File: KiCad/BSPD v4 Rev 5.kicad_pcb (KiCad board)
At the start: 4 copper layers, 100 x 77.5 mm, 194 parts, among them J1 DTM13-12PA, U1 LM339, U10 2N7002, U11 2N7002, U12 2N7002, U13 2N7002, U14 2N7002, U15 2N7002, U16 2N7002, U17 74HC08D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

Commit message: Changed DTM NPTH size
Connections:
- U18 pad 11: (no net) -> unconnected-(U18-Pad11)
- U18 pad 3: (no net) -> unconnected-(U18-Pad3)
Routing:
- net BSPD_status(12V): track 79.0 -> 93.1 mm
- net Net-(U2C--): track 112.2 -> 118.8 mm
- net GND: vias 279 -> 278
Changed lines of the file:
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@@
 			(outputformat 1)
 			(mirror no)
-			(drillshape 1)
+			(drillshape 0)
 			(scaleselection 1)
-			(outputdirectory "")
+			(outputdirectory "../Production/Fab (gerber) BSPD v4 Rev 5/")
 		)
 	)
@@
 	(net 113 "unconnected-(U25C-Q3-Pad10)")
 	(net 114 "unconnected-(U25B-Q2-Pad9)")
+	(net 115 "unconnected-(U18-Pad3)")
+	(net 116 "unconnected-(U18-Pad11)")
 	(footprint "Resistor_SMD:R_0805_2012Metric_Pad1.20x1.40mm_HandSolder"
 		(layer "F.Cu")
@@
 			(at -8.89 -12.7 90)
 			(size 5 5)
-			(drill 3)
-			(layers "F&B.Cu" "*.Mask")
+			(drill 5)
+			(layers "*.Mask")
 		)
 		(pad "" np_thru_hole circle
 			(at 8.89 -12.7 90)
 			(size 5 5)
-			(drill 3)
-			(layers "F&B.Cu" "*.Mask")
+			(drill 5)
+			(layers "*.Mask")
 		)
 		(pad "1" thru_hole roundrect
@@
 		)
 		(group ""
-			(members "0762a500-42f2-42fb-a078-6c1aa5e056fa" "084b3688-b081-4450-aacb-739ad2118ab8"
-				"0d6cd142-b1c8-48ca-ac65-122be22d51ec" "198ef3f8-6b8f-4339-8e8e-52dd78860bf9"
-				"20b9208b-f209-438b-9e0c-cbd13adca767" "492f48d9-6674-48c5-9826-66c5159c251b"
-				"49af12c1-a1eb-4583-9b77-ae47ca6a3e2e" "651534ea-3f12-4366-9872-520313e98250"
-				"7ad67e8d-3dc0-490f-9ea3-ee7503f5d862" "7db140bb-23d2-4ea7-861f-e28e8502dec4"
-				"848d9453-0247-48af-83de-b9f01f822996" "8ba0055a-b60d-4a51-a8c9-ef2f70b57686"
-				"99198183-94ea-4d01-9891-043bd2b0469f" "ab4a9615-9050-4230-b962-8291ca35c75c"
-				"bc787465-82ed-4e8a-a340-4af8fc745ab3" "bda766bf-56de-4e9e-a06b-fc5527dfb734"
-				"d74cc8b5-ec6e-48dc-a64b-0fa3fd9d8ad2" "d878d63a-22b1-43e1-82f4-1738e3ae9442"
-				"db3fa60b-dd23-4084-b817-4ca42268c97e" "e277162a-7d40-42ac-b809-249cfe4dc1e0"
-				"e35fbb23-64cf-4d94-aa0a-6c12e2d1ecf5" "e5b0d9e6-d4bd-4c73-8cac-be1be8c46e06"
+			(members "2a8d6c05-4f68-4065-8f50-f404b86ca30a" "2b647277-423f-45bb-b5af-bc07fde5212c"
+				"2bddd831-3458-409e-bcb9-7c070f0f1419" "32dc1de1-0e17-4066-abfa-8d649ab330a1"
+				"4bfcb310-1cd9-4686-b639-f17e350bee0d" "4d9337d3-cba9-47d8-9d35-7dbac8836a1c"
+				"827f3cdf-d24f-4c54-822c-144fb845f094" "8bbaeb87-f568-4227-8b07-fff5f8ed2c97"
+				"916b219d-f275-4fb5-b2ef-d5d6e7277683" "94bab4a8-2b81-48eb-b3a7-0c39814db9f9"
+				"94d2f2b8-f4b8-45f6-899a-d1736687bf8b" "9807fecc-2b0b-49ce-8c03-c772a7bd696e"
+				"ab198cf8-ebde-45a8-8071-e6fe45066953" "d2159468-2c08-406f-827d-736941325d98"
+				"d5026557-77fd-4762-9f81-bd560b215afa" "e3873f4e-5db2-4c4e-a76c-aa21f2ea86fa"
+				"eb1fc0db-555f-4578-958b-a648d1696b06" "f213b850-67e0-4ee2-b7f8-166f49001d37"
+				"f22a5232-f775-44e7-a3a7-72842215190f" "fd43b7fc-b80b-4804-a2f5-b0c0e8812592"
+				"fda41aae-57ef-41ab-9ef1-84b8804f4714" "ff72e685-8ea9-41a7-82c6-c40ddcfb733d"
 			)
 		)
@@
 			(layers "F.Cu" "F.Mask" "F.Paste")
 			(roundrect_rratio 0.25)
+			(net 115 "unconnected-(U18-Pad3)")
 			(pinfunction "3")
 			(pintype "no_connect")
@@
 			(layers "F.Cu" "F.Mask" "F.Paste")
 			(roundrect_rratio 0.25)
+			(net 116 "unconnected-(U18-Pad11)")
 			(pinfunction "11")
 			(pintype "no_connect")
@@
 	)
 	(via
-		(at 177.4 112.7)
-		(size 0.6)
-		(drill 0.3)
-		(layers "F.Cu" "B.Cu")
-		(free yes)
-		(net 1)
-	)
-	(via
 		(at 179 77)
 		(size 0.6)
@@
 	)
 	(segment
-		(start 151.65 112.54)
-		(end 150.289 113.901)
-		(width 0.2)
-		(layer "F.Cu")
-		(net 21)
-	)
-	(segment
 		(start 169.25 139.05)
 		(end 177.8 139.05)
@@
 	)
 	(segment
-		(start 150.289 113.901)
-		(end 150.289 131.039)
-		(width 0.2)
-		(layer "F.Cu")
-		(net 21)
-	)
-	(segment
 		(start 201.755888 136.55)
 		(end 200.827944 137.477944)
@@
 	)
 	(segment
-		(start 158.3 139.05)
-		(end 169.25 139.05)
-		(width 0.2)
-		(layer "F.Cu")
-		(net 21)
-	)
-	(segment
 		(start 180.25 141.5)
 		(end 180.5 141.5)
@@
 	)
 	(segment
-		(start 150.289 131.039)
-		(end 158.3 139.05)
+		(start 180.25 141.5)
+		(end 177.75 139)
 		(width 0.2)
-		(layer "F.Cu")
+		(layer "In2.Cu")
+		(net 21)
+	)
+	(segment
+		(start 149.5 114.69)
+		(end 151.65 112.54)
+		(width 0.2)
+		(layer "In2.Cu")
+		(net 21)
+	)
+	(segment
+		(start 180.5 141.5)
+		(end 180.25 141.5)
+		(width 0.2)
+		(layer "In2.Cu")
+		(net 21)
+	)
+	(segment
+		(start 156.25 139)
+		(end 149.5 132.25)
+		(width 0.2)
+		(layer "In2.Cu")
+		(net 21)
+	)
+	(segment
+		(start 149.5 132.25)
+		(end 149.5 114.69)
+		(width 0.2)
+		(layer "In2.Cu")
+		(net 21)
+	)
+	(segment
+		(start 177.75 139)
+		(end 156.25 139)
+		(width 0.2)
+		(layer "In2.Cu")
 		(net 21)
 	)
@@
 	)
 	(segment
-		(start 149 131.75)
-		(end 149 106.8)
+		(start 149.4 106.4)
+		(end 151.65 104.15)
 		(width 1)
 		(layer "In1.Cu")
@@
 	)
 	(segment
-		(start 185.15 141.5)
-		(end 182.4 138.75)
+		(start 149.4 132.15)
+		(end 149.4 106.4)
 		(width 1)
 		(layer "In1.Cu")
@@
 	(segment
 		(start 156 138.75)
-		(end 149 131.75)
+		(end 149.4 132.15)
 		(width 1)
 		(layer "In1.Cu")
@@
 	)
 	(segment
-		(start 149 106.8)
-		(end 151.65 104.15)
+		(start 185.15 141.5)
+		(end 182.4 138.75)
 		(width 1)
 		(layer "In1.Cu")
@@
 	)
 	(segment
-		(start 158.75 141.5)
-		(end 174.2 141.5)
+		(start 149.4 110.6)
+		(end 149.4 132.15)
 		(width 1)
 		(layer "F.Cu")
@@
 	)
 	(segment
-		(start 149 131.75)
-		(end 158.75 141.5)
+		(start 151.65 108.35)
+		(end 149.4 110.6)
 		(width 1)
 		(layer "F.Cu")
@@
 	)
 	(segment
-		(start 149 111)
-		(end 149 131.75)
+		(start 149.4 132.15)
+		(end 158.75 141.5)
 		(width 1)
 		(layer "F.Cu")
@@
 	)
 	(segment
-		(start 151.65 108.35)
-		(end 149 111)
+		(start 158.75 141.5)
+		(end 174.2 141.5)
 		(width 1)
 		(layer "F.Cu")
@@
 	)
 	(segment
-		(start 174.04 109.54)
-		(end 174.5 110)
+		(start 226 83.75)
+		(end 227 84.75)
 		(width 0.2)
 		(layer "F.Cu")
@@
 	)
 	(segment
-		(start 174.5 110)
-		(end 176 110)
+		(start 171.5 111.5)
+		(end 172.5 111.5)
 		(width 0.2)
 		(layer "F.Cu")
@@
 	)
 	(segment
-		(start 226 83.75)
-		(end 227 84.75)
+		(start 172.5 111.5)
+		(end 174.04 109.96)
 		(width 0.2)
 		(layer "F.Cu")
@@
 	)
 	(segment
-		(start 174.04 108.725)
-		(end 174.04 109.54)
+		(start 214.416667 71.75)
+		(end 217 71.75)
 		(width 0.2)
 		(layer "F.Cu")
@@
 	)
 	(segment
-		(start 214.416667 71.75)
-		(end 217 71.75)
+		(start 174.04 109.96)
+		(end 174.04 108.725)
 		(width 0.2)
 		(layer "F.Cu")
@@
 	)
 	(via
-		(at 176 110)
+		(at 171.5 111.5)
 		(size 0.6)
 		(drill 0.3)
@@
 	)
 	(segment
-		(start 227 85.5)
+		(start 227 75.25)
 		(end 227 84.75)
 		(width 0.2)
@@
 	)
 	(segment
-		(start 227 75.25)
-		(end 227 84.75)
+		(start 233 91.5)
+		(end 233 102)
 		(width 0.2)
 		(layer "In2.Cu")
@@
 	)
 	(segment
-		(start 233 91.5)
+		(start 227 84.75)
 		(end 227 85.5)
 		(width 0.2)
@@
 	)
 	(segment
+		(start 233 102)
+		(end 225.5 109.5)
+		(width 0.2)
+		(layer "In2.Cu")
+		(net 59)
+	)
+	(segment
 		(start 217 71.75)
 		(end 223.5 71.75)
@@
 	)
 	(segment
-		(start 233 102)
-		(end 233 91.5)
+		(start 172.5 111.5)
+		(end 171.5 111.5)
 		(width 0.2)
 		(layer "In2.Cu")
@@
 	)
 	(segment
-		(start 176 110)
-		(end 176.5 109.5)
+		(start 223.5 71.75)
+		(end 227 75.25)
 		(width 0.2)
 		(layer "In2.Cu")
@@
 	)
 	(segment
-		(start 176.5 109.5)
-		(end 225.5 109.5)
+		(start 225.5 109.5)
+		(end 174.5 109.5)
 		(width 0.2)
 		(layer "In2.Cu")
@@
 	)
 	(segment
-		(start 223.5 71.75)
-		(end 227 75.25)
+		(start 174.5 109.5)
+		(end 172.5 111.5)
 		(width 0.2)
 		(layer "In2.Cu")
@@
 	)
 	(segment
-		(start 225.5 109.5)
-		(end 233 102)
+		(start 227 85.5)
+		(end 233 91.5)
 		(width 0.2)
 		(layer "In2.Cu")

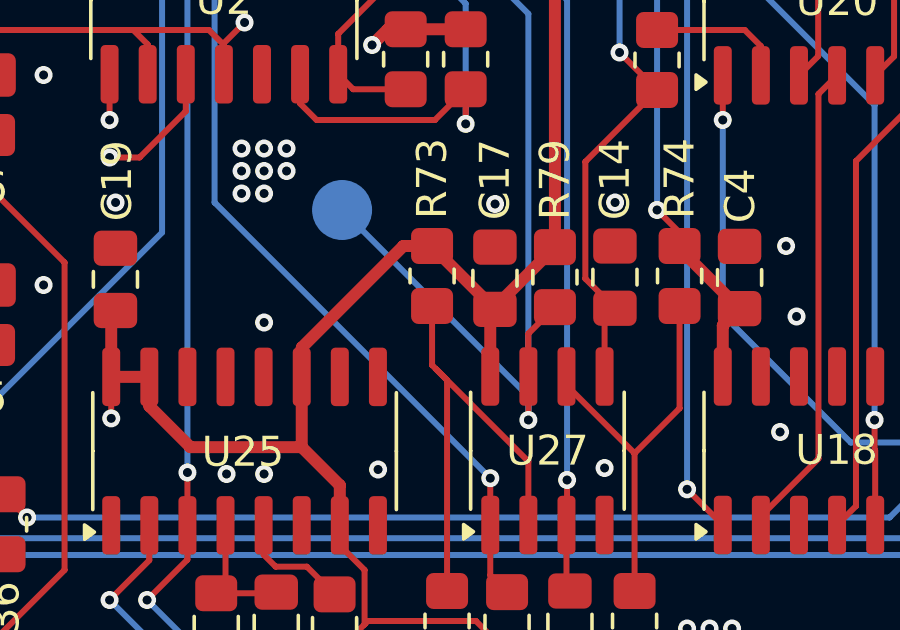
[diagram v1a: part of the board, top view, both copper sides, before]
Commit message: moved lm393 to 12v
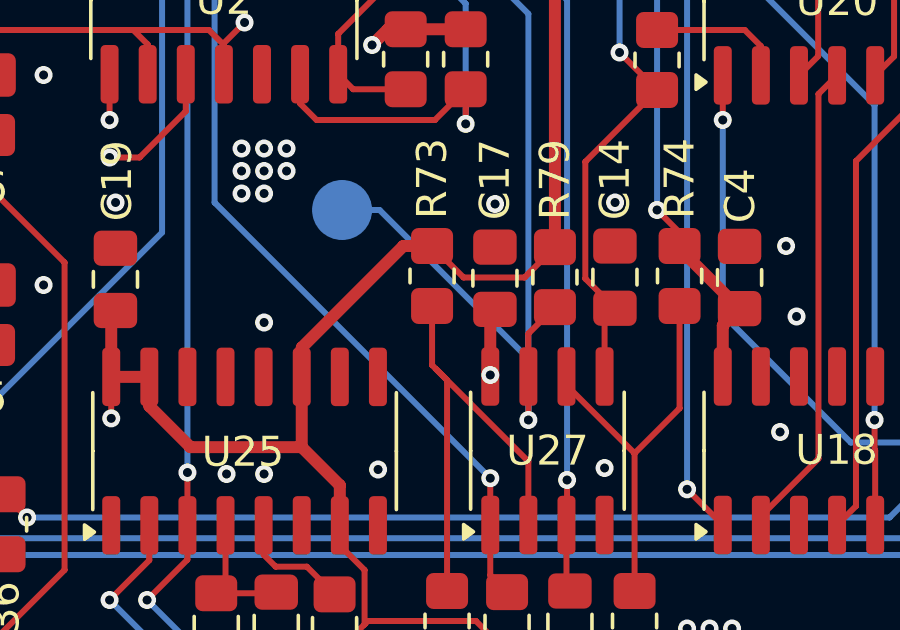
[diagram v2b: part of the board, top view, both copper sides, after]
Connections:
- C17 pad 1: +5V -> +12V
- U27 pad 8: +5V -> +12V
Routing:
- net +12V: track 303.8 -> 322.4 mm, vias 4 -> 5
- net +5V: track 533.6 -> 530.4 mm
- net Net-(U21C-3B): track 48.4 -> 49.1 mm
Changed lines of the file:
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@@
 			(drillshape 0)
 			(scaleselection 1)
-			(outputdirectory "../Production/Fab (gerber) BSPD v4 Rev 5/")
+			(outputdirectory "../Production/Fab/")
 		)
 	)
@@
 			(layers "F.Cu" "F.Mask" "F.Paste")
 			(roundrect_rratio 0.25)
-			(net 2 "+5V")
+			(net 6 "+12V")
 			(pinfunction "V+")
 			(pintype "power_in")
@@
 			(layers "F.Cu" "F.Mask" "F.Paste")
 			(roundrect_rratio 0.212766)
-			(net 2 "+5V")
+			(net 6 "+12V")
 			(pintype "passive")
 		)
@@
 	)
 	(segment
-		(start 184.345 116.4875)
-		(end 186.345 114.4875)
-		(width 0.4)
-		(layer "F.Cu")
-		(net 2)
-	)
-	(segment
 		(start 155 80.5)
 		(end 158.25 77.25)
@@
 	)
 	(segment
-		(start 184.19 118.8)
-		(end 184.19 116.7175)
-		(width 0.4)
-		(layer "F.Cu")
-		(net 2)
-	)
-	(segment
 		(start 187.59375 103.90625)
 		(end 187.6875 103.8125)
@@
 	)
 	(segment
-		(start 182.25 114.4675)
-		(end 184.345 116.5625)
-		(width 0.4)
-		(layer "F.Cu")
-		(net 2)
-	)
-	(segment
 		(start 179 128.0625)
 		(end 177.055 128.0625)
@@
 	)
 	(segment
-		(start 184.19 116.7175)
-		(end 184.345 116.5625)
-		(width 0.4)
-		(layer "F.Cu")
-		(net 2)
-	)
-	(segment
 		(start 204.5 112.78)
 		(end 206.22 114.5)
@@
 	)
 	(segment
+		(start 182.25 114.45)
+		(end 183.3 115.5)
+		(width 0.2)
+		(layer "F.Cu")
+		(net 2)
+	)
+	(segment
 		(start 224 118.25)
 		(end 224 121.25)
@@
 	)
 	(segment
-		(start 184.345 116.5625)
-		(end 184.345 116.4875)
-		(width 0.4)
-		(layer "F.Cu")
-		(net 2)
-	)
-	(segment
 		(start 155.44 132.5)
 		(end 157.44 132.5)
@@
 	)
 	(segment
+		(start 185.3325 115.5)
+		(end 186.345 114.4875)
+		(width 0.2)
+		(layer "F.Cu")
+		(net 2)
+	)
+	(segment
 		(start 224 93.25)
 		(end 224.5 93.75)
@@
 	)
 	(segment
+		(start 183.3 115.5)
+		(end 185.3325 115.5)
+		(width 0.2)
+		(layer "F.Cu")
+		(net 2)
+	)
+	(segment
 		(start 224 116.735)
 		(end 226.235 114.5)
@@
 	)
 	(segment
+		(start 184.19 118.75)
+		(end 184.19 116.7175)
+		(width 0.4)
+		(layer "F.Cu")
+		(net 6)
+	)
+	(segment
 		(start 204 102.3)
 		(end 204.5 102.8)
@@
 	)
 	(segment
+		(start 184.19 118.8)
+		(end 184.19 118.75)
+		(width 0.4)
+		(layer "F.Cu")
+		(net 6)
+	)
+	(segment
 		(start 156.75 136.25)
 		(end 165.5 136.25)
@@
 	)
 	(segment
+		(start 184.19 116.7175)
+		(end 184.345 116.5625)
+		(width 0.4)
+		(layer "F.Cu")
+		(net 6)
+	)
+	(segment
 		(start 158.73 129.63)
 		(end 159.5 130.4)
@@
 	)
 	(segment
+		(start 184.345 116.5625)
+		(end 184.345 116.4875)
+		(width 0.4)
+		(layer "F.Cu")
+		(net 6)
+	)
+	(segment
 		(start 151.77 116.73)
 		(end 154 114.5)
@@
 	)
 	(via
+		(at 184.19 118.75)
+		(size 0.6)
+		(drill 0.3)
+		(layers "F.Cu" "B.Cu")
+		(net 6)
+	)
+	(via
 		(at 161.21 84.3)
 		(size 0.6)
@@
 	)
 	(segment
+		(start 182.75 120.19)
+		(end 182.75 131.25)
+		(width 0.4)
+		(layer "In2.Cu")
+		(net 6)
+	)
+	(segment
+		(start 182.75 131.25)
+		(end 180.5 133.5)
+		(width 0.4)
+		(layer "In2.Cu")
+		(net 6)
+	)
+	(segment
+		(start 184.19 118.75)
+		(end 182.75 120.19)
+		(width 0.4)
+		(layer "In2.Cu")
+		(net 6)
+	)
+	(segment
 		(start 204.5 102.8)
 		(end 206.7 105)
@@
 	(segment
 		(start 179.25 113.25)
-		(end 185.46 119.46)
+		(end 180.5 113.25)
 		(width 0.2)
 		(layer "B.Cu")
@@
 	)
 	(segment
-		(start 185.46 119.46)
+		(start 180.5 113.25)
+		(end 185.46 118.21)
+		(width 0.2)
+		(layer "B.Cu")
+		(net 90)
+	)
+	(segment
+		(start 185.46 118.21)
 		(end 185.46 120.25)
 		(width 0.2)

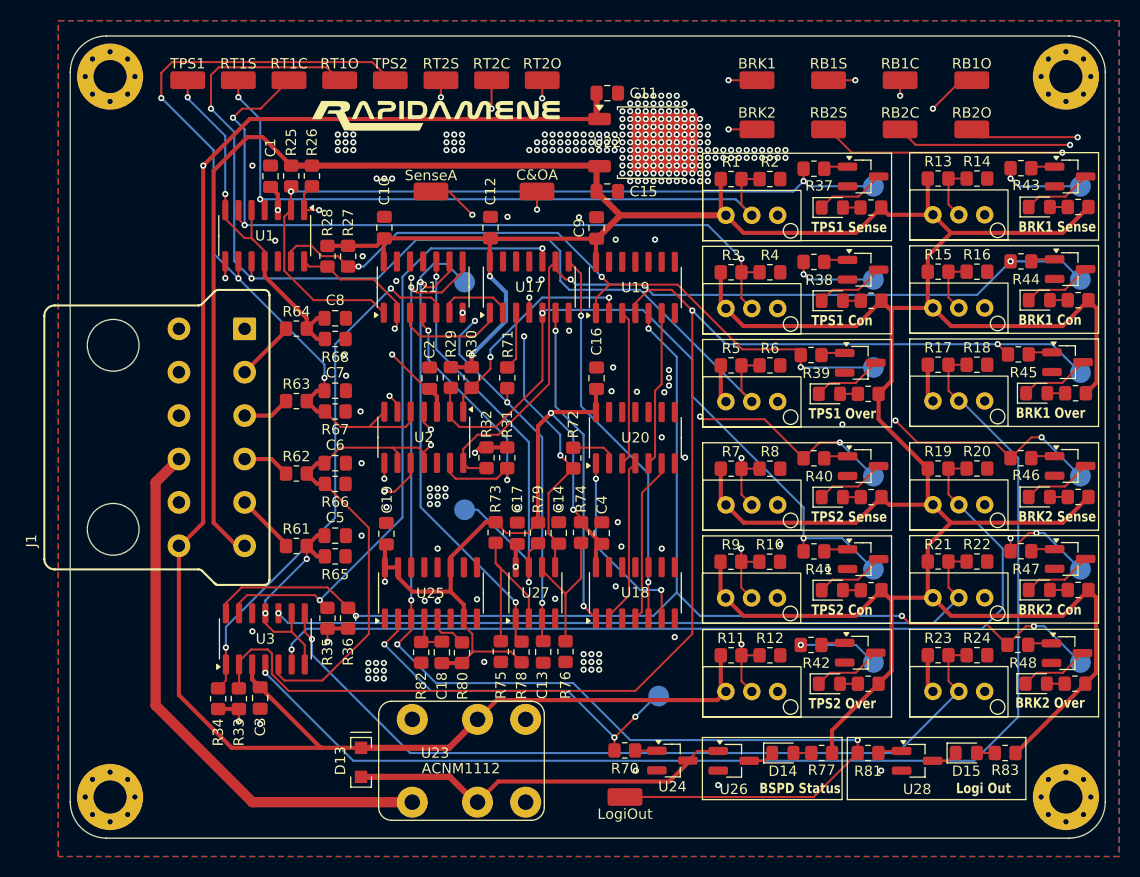
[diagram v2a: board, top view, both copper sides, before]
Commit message: differentail TPS, stable Over ref voltage
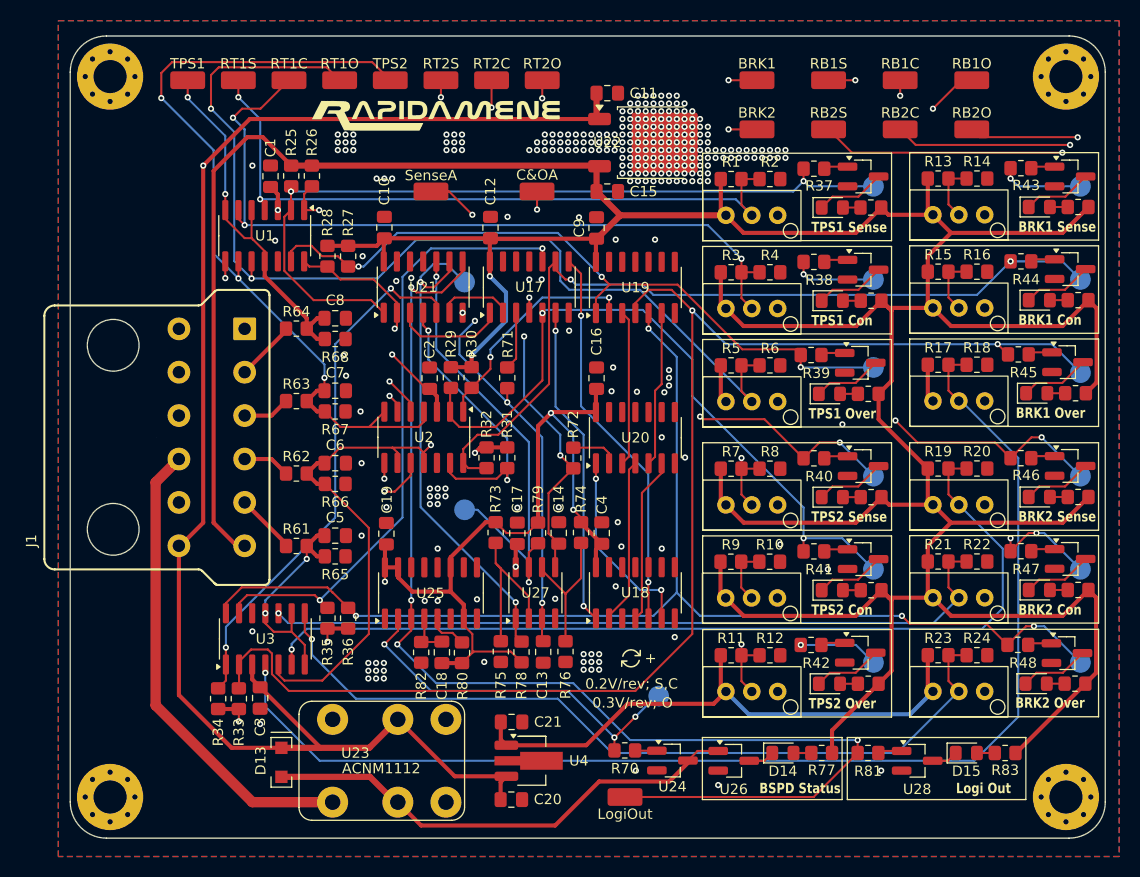
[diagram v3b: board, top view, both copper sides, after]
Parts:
- added C20: C0.33uF, Capacitor_SMD:C_0805_2012Metric_Pad1.18x1.45mm_HandSolder, F.Cu at (183.8, 141.2)
- added C21: C0.1uF, Capacitor_SMD:C_0805_2012Metric_Pad1.18x1.45mm_HandSolder, F.Cu at (183.8, 133.8)
- added U4: 78L08MG-AB3-R, Package_TO_SOT_SMD:SOT-89-3_Handsoldering, F.Cu at (185.7, 137.5)
- moved D13 7.70 mm to (161.6, 137.5)
- moved U23 7.70 mm to (171.3, 137.5)
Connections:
- R10 pad 1: Net-(U2A--) -> Net-(U2A-+)
- R11 pad 1: +12V -> +8V
- R17 pad 1: +12V -> +8V
- R23 pad 1: +12V -> +8V
- R5 pad 1: +12V -> +8V
- R9 pad 2: Net-(U2A--) -> Net-(U2A-+)
- RV12 pad 1: +12V -> +8V
- RV3 pad 1: +12V -> +8V
- RV5 pad 2: Net-(U2A--) -> Net-(U2A-+)
- RV6 pad 1: +12V -> +8V
- RV9 pad 1: +12V -> +8V
- TP7 pad 1: Net-(U2A--) -> Net-(U2A-+)
- U2 pad 4: Net-(U2A--) -> TPS2
- U2 pad 5: TPS2 -> Net-(U2A-+)
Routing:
- net +12V: track 322.4 -> 205.3 mm, vias 5 -> 4
- net +8V: track 0.00 -> 113.8 mm, vias 0 -> 1
- net Net-(U2A-+): track 0.00 -> 88.5 mm, vias 0 -> 2
- net Net-(U2A--): track 85.5 -> 0.00 mm, vias 3 -> 0
- net Relay_com: track 102.2 -> 86.8 mm
- net Relay_NC: track 68.1 -> 60.4 mm
- net Relay_NO: track 68.6 -> 60.9 mm
- net Net-(U3A--): track 160.2 -> 162.1 mm
- net BSPD_status(12V): track 93.1 -> 94.7 mm
- net TPS2: track 78.6 -> 79.9 mm
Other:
- board text added: "+"
- board text added: "0.2V/rev; S,C"
- board text added: "0.3V/rev; O"
